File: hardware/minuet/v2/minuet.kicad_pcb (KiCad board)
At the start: 2 copper layers, 79 x 79 mm, 93 parts, among them J101 B2P-VH-B, J102 B2B-XH-A, J103 PPPC062LFBN-RC, J104 B2B-XH-A, J201 USB4105-GF-A, J202 SM04B-SRSS-TB, J301 B3P-VH-B, J302 B5B-XH-A, J401 B2B-XH-A, J501 G800LE300018YEU, J502 MTJ-889X1, J503 MTJ-669X1, Q101 MMBT3904, SW201 EVQ-P7A01P, SW202 EVQ-P7A01P, U101 TSOP39238, U102 LMV331X-SC5R, U201 TCA9555RTWR, U202 ESP32-C3-WROOM-02, U301 MCT8315Z0HRRYR, U401 DRV8876PWPR

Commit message: Finishing touches for v2.
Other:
- board text added: "github.com/j9brown/minuet Brown Studios Minuet Fan Controller 2025/2, v2.0"
- board text removed: "github.com/j9brown/minuet Brown Studios Minuet Fan Controller 2024/2, v2.0"

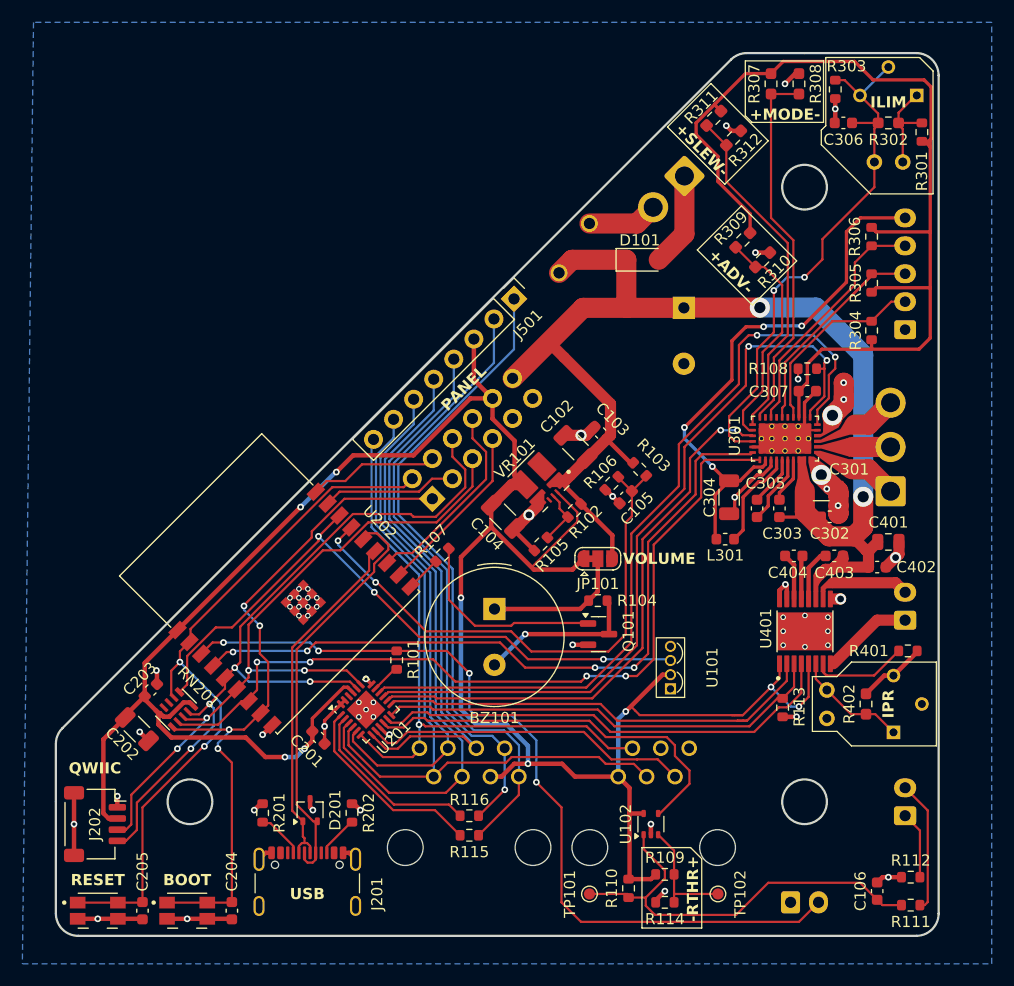
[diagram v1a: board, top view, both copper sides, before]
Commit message: Finalize Minuet v2.1 for manufacture.
This revision uses a different motor controller and buck converter
and remedies errata from v2.0.
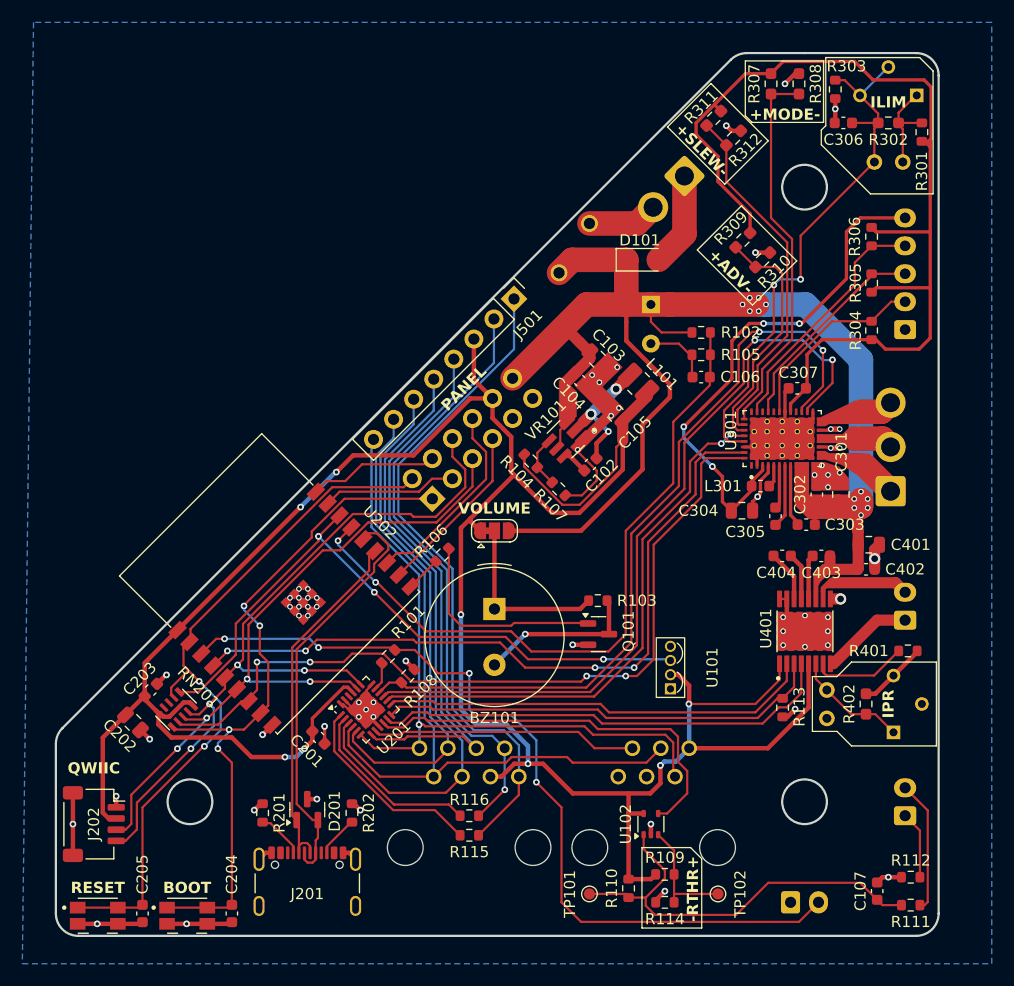
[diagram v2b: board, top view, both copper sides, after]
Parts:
- removed the NT102 at (75.8, 78.8)
- removed NT402: NetTie_2, Generic:NetTie-2_SMD_Pad0.2mm
- removed the R102 at (79.4, 73.9)
- removed the R105 at (76.4, 76.9)
- added C102: 100n, Capacitor_SMD:C_0603_1608Metric, F.Cu at (80.8, 69.8)
- added L101: 3.3u, Inductor_SMD:L_1008_2520Metric, F.Cu at (85.1, 62.6)
- added NT101: NetTie_2, Generic:NetTie-2_SMD_Pad0.2mm, F.Cu at (86.2, 56.8)
- added NT103: NetTie_2, Generic:NetTie-2_SMD_Pad0.4mm, F.Cu at (84.0, 56.8)
- added R104: 33.2K, Resistor_SMD:R_0603_1608Metric, F.Cu at (75.5, 69.5)
- added R107: 10K, Resistor_SMD:R_0603_1608Metric, F.Cu at (78.0, 72.0)
- C101: value 1000u -> 680u; footprint Capacitor_THT:CP_Radial_D10.0mm_P5.00mm -> Capacitor_THT:CP_Radial_D8.0mm_P3.50mm
- C103: renamed from C102; value 10u -> 22u; footprint Capacitor_SMD:C_1206_3216Metric -> Capacitor_SMD:C_0805_2012Metric
- C105: renamed from C104; value 22u -> 47u; footprint Capacitor_SMD:C_1206_3216Metric -> Capacitor_SMD:C_0805_2012Metric
- C106: renamed from C105; value 1u -> 100n
- C202, C304: footprint Capacitor_SMD:C_1206_3216Metric -> Capacitor_SMD:C_0805_2012Metric
- C301: value 10u -> 22u; footprint Capacitor_SMD:C_1206_3216Metric -> Capacitor_SMD:C_0805_2012Metric
- D101: value SMF16A-E3-08 -> SMF16A
- D201: value DF3A5.6LFU -> PESD3V3S2UT; footprint Package_TO_SOT_SMD:SOT-323_SC-70 -> Package_TO_SOT_SMD:SOT-23
- F101: value RGEF400K-2 -> RGEF400K
- R301, R303: value 10K -> 18.2K
- R302: value 3.40K -> 3.65K
- SW201, SW202: value EVQ-P7A01P -> EVQ-P7J01P
- U102: value LMV331X-SC5R -> LMV331IDCK
- U201: value TCA9555RTWR -> TCA9555RTW
- U202: value ESP32-C3-WROOM-02 -> ESP32-C3-WROOM-02-N4
- U301: value MCT8315Z0HRRYR -> MCT8316Z0T; footprint MCT8315Z:IC_MCT8315Z0HRRYR -> MCT8316Z:MCT8316ZT
- U401: value DRV8876PWPR -> DRV8876PWP
- VR101: value TPSM861253RDXR -> TPS561201DDCR; footprint TPSM861253RDXR:VREG_TPSM861253RDXR -> TPS561201:SOT95P280X110-6N
- moved R108 45.1 mm to (64.5, 88.8), turned to -135 degrees
- moved R105 14.0 mm to (90.8, 60.0), turned to 0 degrees
- moved C105 13.7 mm to (83.1, 65.2), turned to 135 degrees
- moved R102 13.4 mm to (90.8, 58.0), turned to 180 degrees
- moved C106 12.7 mm to (90.8, 62.0), turned to 180 degrees
- moved JP101 9.58 mm to (72.2, 75.8)
- moved C103 8.10 mm to (81.5, 60.4), turned to -45 degrees
- moved L301 5.70 mm to (96.0, 71.8)
- moved C104 5.04 mm to (79.9, 62.3), turned to -45 degrees
- moved VR101 4.47 mm to (78.6, 67.6)
- moved C101 2.97 mm to (86.2, 55.5)
- moved C303 2.80 mm to (100.2, 75.2), turned to 180 degrees
- moved C302 2.31 mm to (101.1, 72.5), turned to 90 degrees
- moved NT401 2.02 mm to (104.8, 75.0), turned to -90 degrees
- moved NT102 1.95 mm to (79.4, 58.4)
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- renumbered C103 to C104, C106 to C107, NT101 to NT102, R103 to R102, R104 to R103, R106 to R105, R107 to R106
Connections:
- C103 pad 1: /12V_PWR -> Net-(VR101-EN)
- C104 pad 1: /12V_PWR -> Net-(VR101-EN)
- J503 pad 1: unconnected-(J503-Pad1) -> +3.3V
- J503 pad 2: XIO7 -> XIO5
- J503 pad 3: GND -> XIO3
- J503 pad 4: XIO3 -> GND
- J503 pad 5: XIO5 -> XIO7
- J503 pad 6: +3.3V -> unconnected-(J503-Pad6)
- JP101 pad 3: /12V_PWR -> Net-(JP101-B)
- NT102 pad 2: /12V_PWR -> Net-(VR101-EN)
- R102 pad 2: /12V_PWR -> Net-(NT101-Pad2)
- R108 pad 2: XIO13 -> XIO14
- U201 pad 19: SDA -> SCL
- U201 pad 20: SCL -> SDA
- U301 pad 1: GPIO8_STRAP -> unconnected-(U301-NC-Pad1)
- U301 pad 10: GND -> +12V
- U301 pad 11: /fan/U -> +12V
- U301 pad 12: /fan/V -> GND
- U301 pad 13: /fan/W -> /fan/U
- U301 pad 14: GND -> /fan/U
- U301 pad 16: XIO14 -> /fan/V
- U301 pad 17: XIO13 -> /fan/V
- U301 pad 19: /fan/AVDD -> /fan/W
- U301 pad 2: /fan/VBK -> GND
- U301 pad 20: /fan/U_HALL -> /fan/W
- U301 pad 21: unconnected-(U301-HNA-Pad21) -> GND
- U301 pad 22: /fan/V_HALL -> XIO13
- U301 pad 23: unconnected-(U301-HNB-Pad23) -> XIO14
- U301 pad 24: /fan/W_HALL -> unconnected-(U301-VSEL_BK-Pad24)
- U301 pad 25: unconnected-(U301-HNC-Pad25) -> /fan/AVDD
- U301 pad 26: /fan/MODE -> GND
- U301 pad 27: /fan/SLEW -> /fan/U_HALL
- U301 pad 28: /fan/ADVANCE -> unconnected-(U301-HNA-Pad28)
- U301 pad 29: XIO12 -> /fan/V_HALL
- U301 pad 3: GND -> /fan/VBK
- U301 pad 30: /fan/ILIM -> unconnected-(U301-HNB-Pad30)
- U301 pad 31: GND -> /fan/W_HALL
- U301 pad 32: GPIO5 -> unconnected-(U301-HNC-Pad32)
- U301 pad 33: GND -> /fan/MODE
- U301 pad 34: GND -> /fan/SLEW
- U301 pad 35: GND -> /fan/ADVANCE
- U301 pad 36: GND -> XIO12
- U301 pad 37: GND -> /fan/ILIM
- U301 pad 39: GND -> GPIO5
- U301 pad 4: Net-(U301-SW_BK) -> GND
- U301 pad 40: GND -> GPIO8_STRAP
- U301 pad 5: Net-(U301-CPL) -> Net-(U301-SW_BK)
- U301 pad 6: Net-(U301-CPH) -> Net-(U301-CPL)
- U301 pad 7: Net-(U301-CP) -> Net-(U301-CPH)
- U301 pad 8: +12V -> Net-(U301-CP)
- U401 pad 1: /cover/VREF -> +3.3V
- U401 pad 5: /cover/VREF -> +3.3V
- VR101 pad 1: /12V_PWR -> GND
- VR101 pad 2: unconnected-(VR101-SW-Pad2) -> Net-(VR101-SW)
- VR101 pad 3: +3.3V -> Net-(VR101-EN)
- VR101 pad 4: GND -> Net-(VR101-VFB)
- VR101 pad 5: unconnected-(VR101-PG-Pad5) -> Net-(VR101-EN)
- VR101 pad 6: /EN -> Net-(VR101-VBST)
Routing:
- net +3.3V: track 180.8 -> 237.8 mm, vias 7 -> 8
- net Net-(JP101-B): track 0.00 -> 30.0 mm
- net /12V_PWR: track 26.8 -> 0.00 mm
- net /cover/VREF: track 24.1 -> 0.00 mm, vias 2 -> 0
- net GPIO3: track 49.0 -> 62.5 mm
- net Net-(VR101-SW): track 0.00 -> 11.0 mm, vias 0 -> 3
- net GND: track 112.1 -> 102.1 mm, vias 61 -> 65
- net Net-(VR101-VOS): track 8.58 -> 0.00 mm
- net Net-(U301-SW_BK): track 8.95 -> 2.02 mm
- net +12V: track 74.1 -> 67.8 mm, vias 2 -> 12
- net XIO5: track 55.0 -> 61.3 mm
- net Net-(VR101-EN): track 0.00 -> 6.14 mm
- net XIO7: track 29.3 -> 23.8 mm
- net /EN: track 5.03 -> 0.00 mm
- net Net-(VR101-VFB): track 0.00 -> 4.70 mm
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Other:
- board text added: "github.com/j9brown/minuet Brown Studios Minuet Fan Controller 2025/2, v2.1"
- board text removed: "github.com/j9brown/minuet Brown Studios Minuet Fan Controller 2025/2, v2.0"
